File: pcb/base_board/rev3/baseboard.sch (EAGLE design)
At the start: 40 parts, among them IC1 LD117AS33TR, P1 RPI3NO-CONNECTORS, SW2 SPST_TACT-EVQQ2, SW5 SPST_TACT-EVQQ2, SW6 SPST_TACT-EVQQ2, SW7 SPST_TACT-EVQQ2, SW8 SPST_TACT-EVQQ2, U5 CH340C

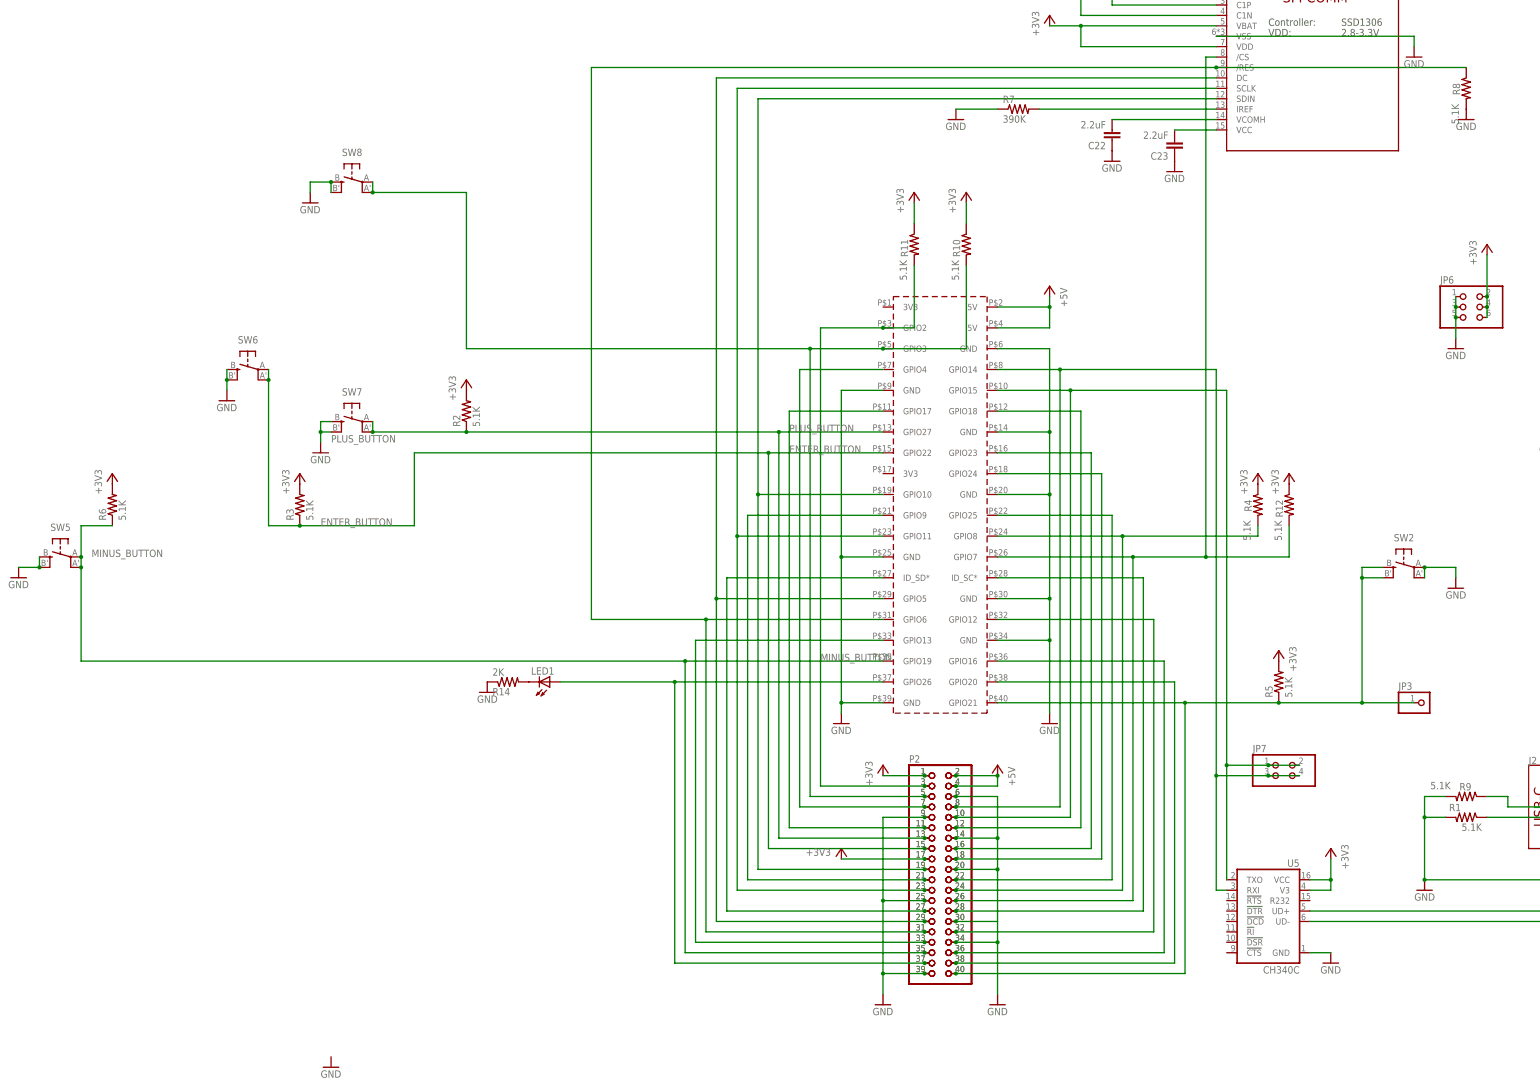
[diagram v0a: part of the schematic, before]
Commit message: new baseboard revision with more sturdy buttons
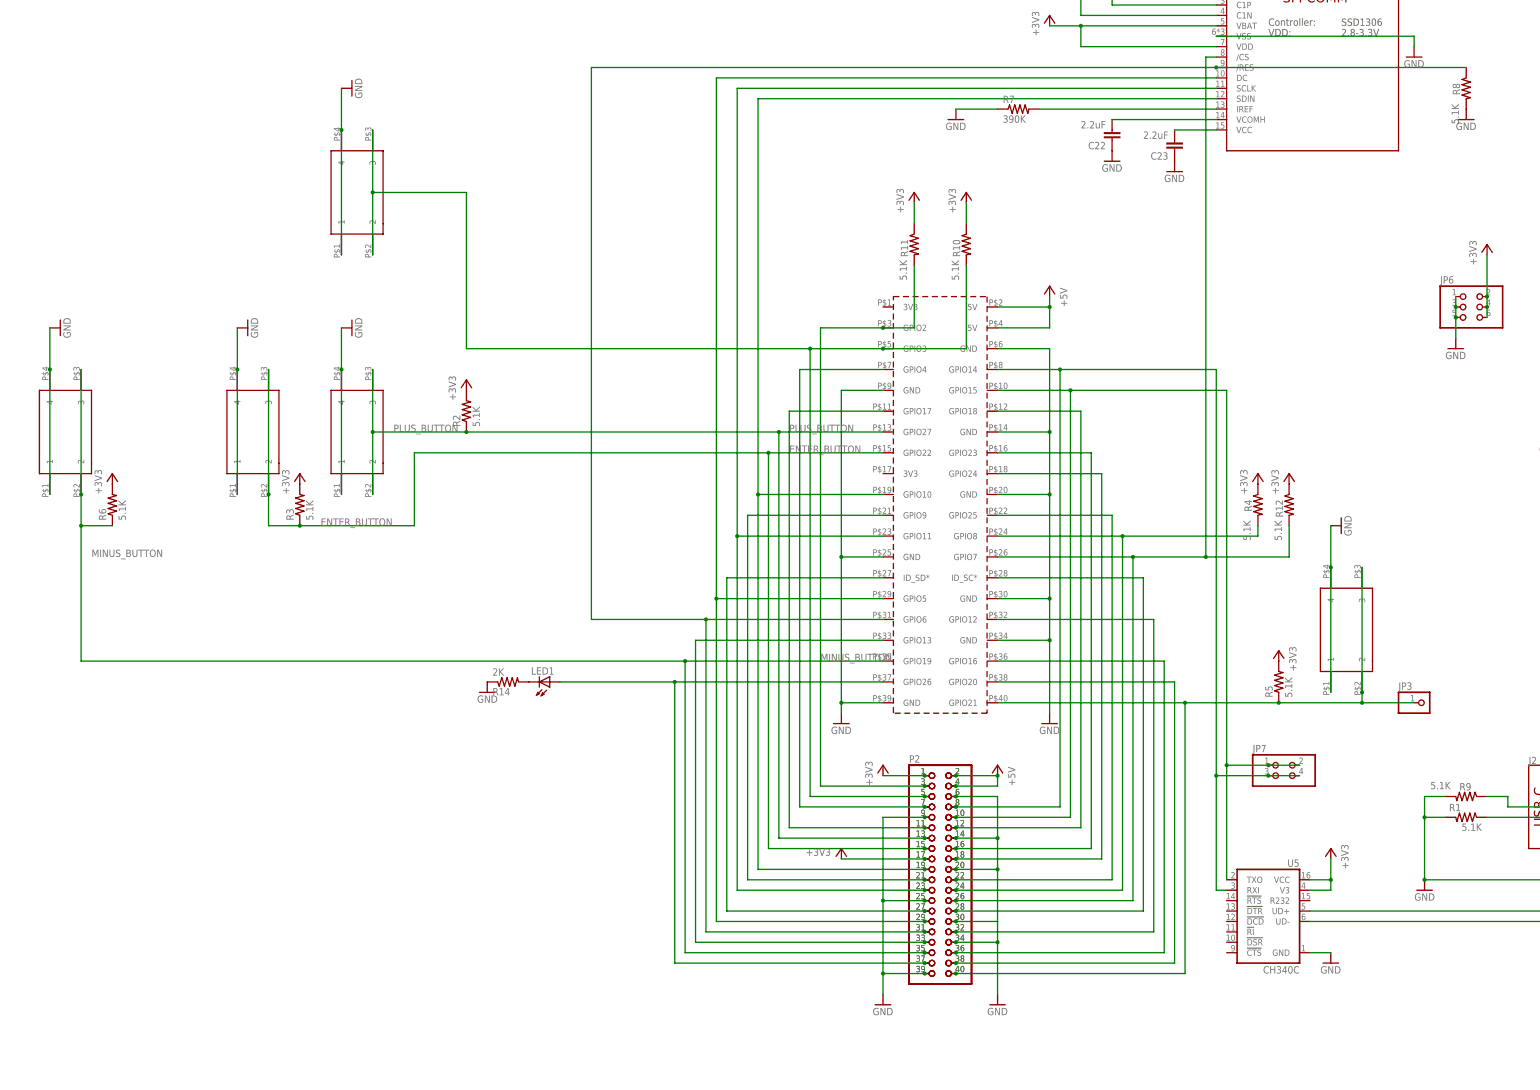
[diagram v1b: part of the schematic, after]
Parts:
- removed SW5, SW6, SW7, SW8: SPST_TACT-EVQQ2, duckypad:SPST_TACT-EVQQ2
- added SW1, SW20, SW3, SW4: 324_SW, 3pos_slide_switch_centered:324_SW
- SW2: value SPST_TACT-EVQQ2 -> 324_SW; device duckypad:SPST_TACT-EVQQ2 -> 3pos_slide_switch_centered:324_SW
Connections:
- net ENTER_BUTTON: now also SW20.2, SW20.3; no longer SW6.P, SW6.P1
- net GND: now also SW1.1, SW1.4, SW2.1, SW2.4, SW20.1, SW20.4, SW3.1, SW3.4, SW4.1, SW4.4; no longer SW2.P, SW2.P1, SW5.S, SW5.S1, SW6.S, SW6.S1, SW7.S, SW7.S1, SW8.S, SW8.S1
- net MINUS_BUTTON: now also SW4.2, SW4.3; no longer SW5.P, SW5.P1
- net N$32: now also SW3.2, SW3.3; no longer SW2.S, SW2.S1
- net N$6: now also SW2.2, SW2.3; no longer SW8.P, SW8.P1
- net PLUS_BUTTON: now also SW1.2, SW1.3; no longer SW7.P, SW7.P1
